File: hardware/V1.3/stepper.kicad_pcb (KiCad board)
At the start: 4 copper layers, 40 x 40 mm, 119 parts, among them J101 USB-MINI-B-SMD, J102 DRILL, J103 DRILL, J104 DRILL, J105 DRILL, J401 STACK-UP-HIGH, J402 STACK-DOWN, J403 STACK-UP-HIGH, J404 STACK-DOWN, P201 black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

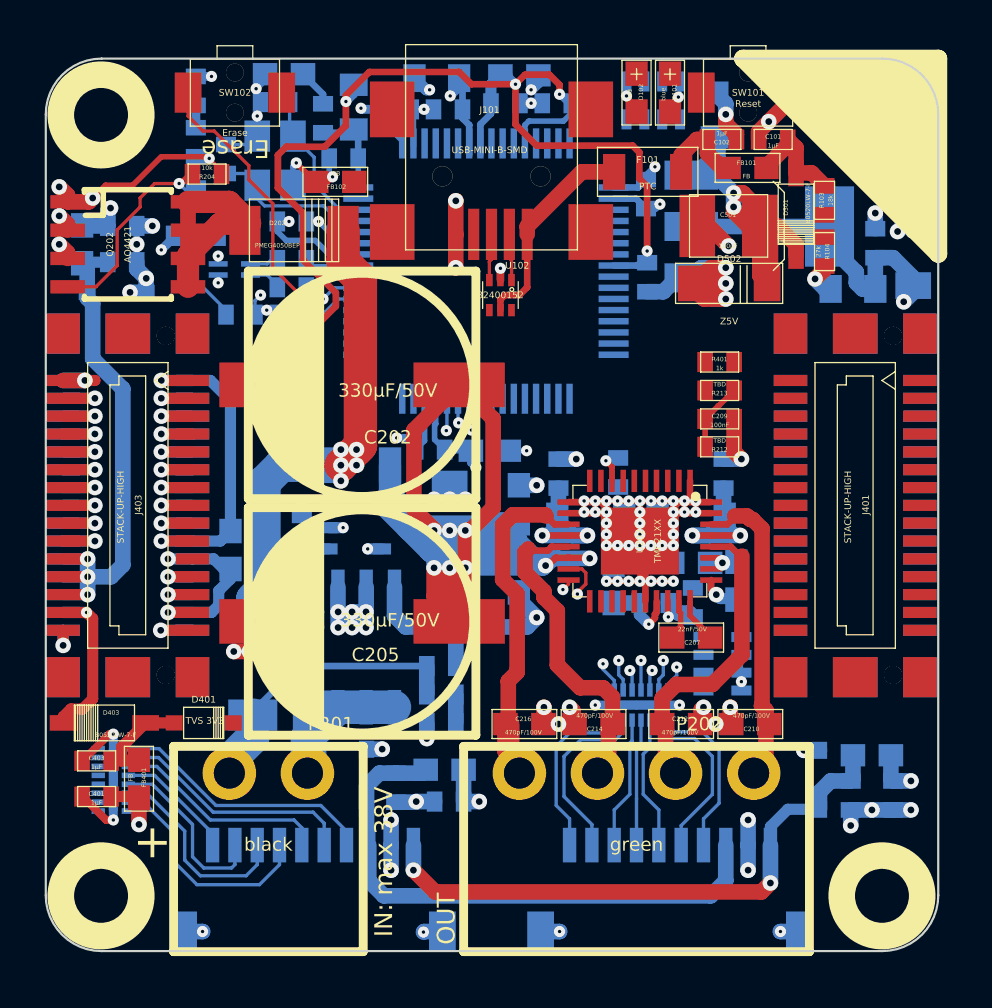
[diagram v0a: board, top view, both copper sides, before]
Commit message: fully routed, fine tuning missing
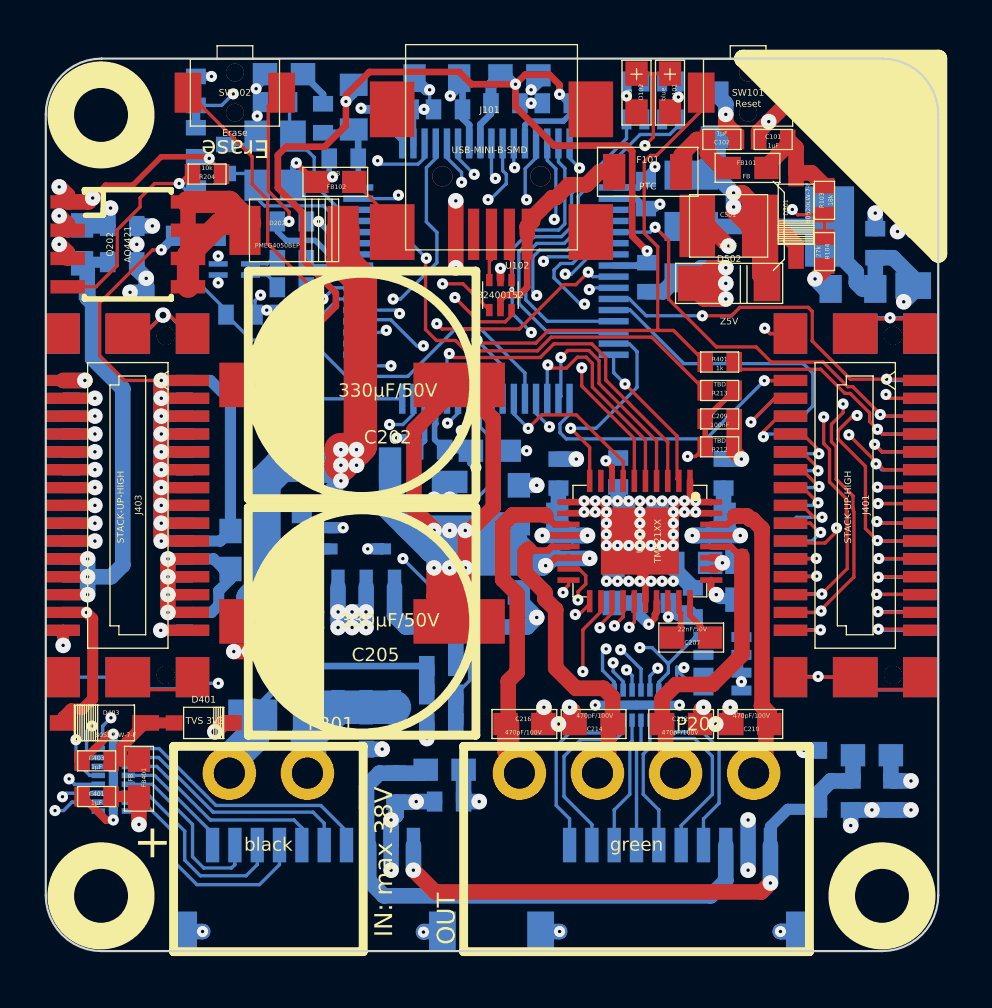
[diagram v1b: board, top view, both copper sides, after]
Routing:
- net GND: track 189.6 -> 402.5 mm, vias 57 -> 63
- net 3V3: track 44.6 -> 192.9 mm, vias 12 -> 14
- net BRICKLET-I2C-SCL: track 1.19 -> 54.6 mm, vias 1 -> 3
- net BRICKLET-I2C-SDA: track 2.35 -> 53.6 mm, vias 2 -> 3
- net BRICKLET-IO0_0/AD0: track 0.00 -> 45.8 mm, vias 0 -> 2
- net BRICKLET-IO1_0/AD1: track 1.33 -> 45.4 mm, vias 1 -> 2
- net BRICKLET-IO0_1: track 0.00 -> 42.0 mm, vias 0 -> 2
- net STACK-INT: track 0.00 -> 40.3 mm, vias 0 -> 3
- net BRICKLET-IO0_3: track 0.00 -> 39.4 mm, vias 0 -> 3
- net STACK-PGND: track 178.0 -> 217.1 mm, vias 78 -> 77
- net STACK-SER-RXD: track 0.00 -> 35.5 mm, vias 0 -> 3
- net STACK-SER-TXD: track 0.00 -> 35.2 mm, vias 0 -> 3
- net BRICKLET-IO1_1: track 0.92 -> 36.0 mm, vias 1 -> 2
- net BRICKLET-IO1_3: track 1.38 -> 33.8 mm, vias 1 -> 2
- net PWR-ENABLE: track 0.00 -> 31.4 mm, vias 0 -> 2
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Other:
- net class Default: trace_width 0.14986 -> 0.148
- rule trace_min: 0.14986 -> 0.148

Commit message: fully routed, logos etc. placed, finished
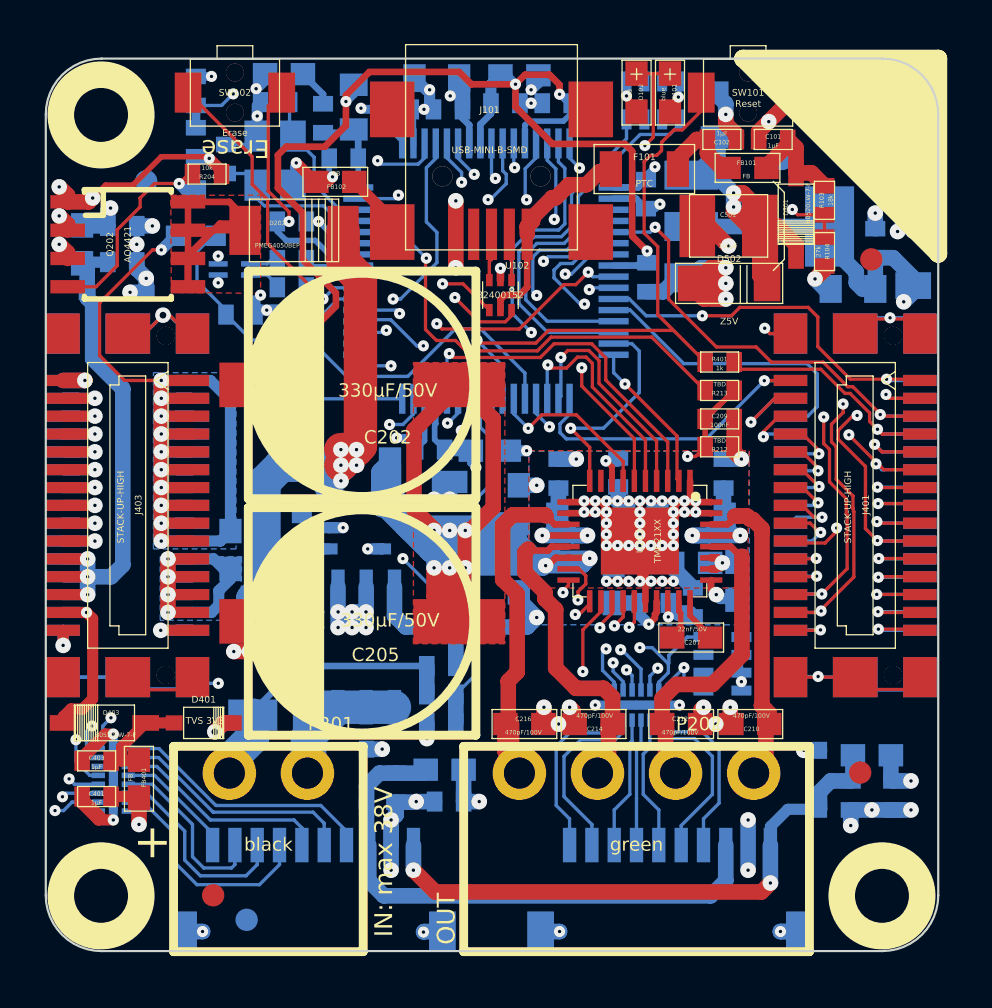
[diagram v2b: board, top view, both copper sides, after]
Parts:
- added Fiducial_Mark: VAL**, kicad-libraries:Fiducial_Mark, F.Cu at (163.7, 81.8)
- added Fiducial_Mark: VAL**, kicad-libraries:Fiducial_Mark, B.Cu at (135.7, 111.4)
- added Fiducial_Mark: VAL**, kicad-libraries:Fiducial_Mark, B.Cu at (131.2, 78.3)
- added Fiducial_Mark: VAL**, kicad-libraries:Fiducial_Mark, B.Cu at (159.7, 77.3)
- added Fiducial_Mark: VAL**, kicad-libraries:Fiducial_Mark, F.Cu at (163.2, 104.8)
- added Fiducial_Mark: VAL**, kicad-libraries:Fiducial_Mark, F.Cu at (134.2, 110.3)
- added G***: LOGO, kicad-libraries:Logo_31x31m, B.Cu at (157.5, 85.2)
- added VAL: WEEE_7mm_back, kicad-libraries:WEEE_7mm_back, B.Cu at (136.3, 88.3)
- added VAL: CE_5mm, kicad-libraries:CE_5mm, B.Cu at (148.4, 101.1)
- moved F101 0.20 mm to (153.6, 77.7)
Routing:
- net GND: track 402.5 -> 435.4 mm
- net VEE: track 73.7 -> 77.8 mm
- net Net-(D202-Pad2): track 28.2 -> 30.2 mm
- net 3V3: track 192.9 -> 192.0 mm
- net BRICKLET-IO1_0/AD1: track 45.4 -> 46.0 mm
- net BRICKLET-I2C-SDA: track 53.6 -> 54.2 mm
- net Net-(L101-Pad3): track 14.6 -> 15.1 mm
- net STACK-RESET: track 26.3 -> 26.8 mm
- added copper zone on VCC, net 3V3
- added copper zone on B.Cu, net GND
- added copper zone on GND, net GND
- added copper zone on F.Cu, net Net-(D202-Pad1)
- added copper zone on B.Cu, net STACK-PGND
- added copper zone on F.Cu, net STACK-PGND
- added copper zone on GND, net STACK-PGND
- added copper zone on VCC, net STACK-PVCC
- added copper zone on F.Cu, net VEE
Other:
- board text added: "tinkerforge.com"
- board text removed: "Reset"

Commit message: ordered version
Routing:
- net M2: track 14.5 -> 15.5 mm
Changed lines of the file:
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@@
     (thickness 1.6002)
     (drawings 64)
-    (tracks 2583)
+    (tracks 2589)
     (zones 0)
     (modules 128)
@@
     (1 GND signal hide)
     (2 VCC signal hide)
-    (31 Rückseite signal hide)
+    (31 Rückseite signal)
     (32 B.Adhes user)
     (33 F.Adhes user)
@@
   )
   (setup
-    (last_trace_width 0.1524)
+    (last_trace_width 0.25)
     (user_trace_width 0.1524)
     (user_trace_width 0.25)
@@
     (pad_to_mask_clearance 0)
     (aux_axis_origin 126.72568 112.776)
-    (visible_elements FFFF5FBF)
+    (visible_elements FFFF9FBF)
     (pcbplotparams
-      (layerselection 0x00030_80000001)
+      (layerselection 0x010f0_80000007)
       (usegerberextensions true)
       (excludeedgelayer true)
       (linewidth 0.150000)
-      (plotframeref true)
+      (plotframeref false)
       (viasonmask false)
       (mode 1)
@@
       (drillshape 0)
       (scaleselection 1)
-      (outputdirectory prod/))
+      (outputdirectory /tmp/stepper/))
   )
   (net 0 "")
@@
   (segment (start 139.15 74.8) (end 139.15 74.3749) (width 0.2998) (layer Rückseite) (net 123))
   (segment (start 139.05 74.6499) (end 139.2 74.8) (width 0.2998) (layer Rückseite) (net 123))
+  (segment (start 157.15 93.6507) (end 157.5257 93.275) (width 0.35) (layer Vorderseite) (net 124))
+  (segment (start 157.6 93.275) (end 157.8 93.275) (width 0.701) (layer Vorderseite) (net 124))
+  (segment (start 157.5257 93.275) (end 157.6 93.275) (width 0.35) (layer Vorderseite) (net 124))
   (segment (start 159.1501 102.6) (end 159.1501 102.1251) (width 0.70104) (layer Vorderseite) (net 124))
   (segment (start 159.1501 102.1251) (end 158.8 101.775) (width 0.70104) (layer Vorderseite) (net 124))
@@
   (segment (start 158.3 93.425) (end 158.3 93.5) (width 0.1524) (layer Vorderseite) (net 124))
   (segment (start 158.3 93.5) (end 158.825 94.025) (width 0.1524) (layer Vorderseite) (net 124))
-  (segment (start 156.54786 93.6507) (end 157.4243 93.6507) (width 0.1524) (layer Vorderseite) (net 124))
-  (segment (start 157.4243 93.6507) (end 157.8 93.275) (width 0.1524) (layer Vorderseite) (net 124))
+  (segment (start 156.54786 93.6507) (end 157.15 93.6507) (width 0.1524) (layer Vorderseite) (net 124))
   (segment (start 158.4 93.425) (end 158.3 93.425) (width 0.701) (layer Vorderseite) (net 124))
   (segment (start 158.15 93.275) (end 157.8 93.275) (width 0.701) (layer Vorderseite) (net 124))
-  (segment (start 157.8 93.275) (end 157.6 93.275) (width 0.701) (layer Vorderseite) (net 124))
   (segment (start 158.3 93.425) (end 158.15 93.275) (width 0.701) (layer Vorderseite) (net 124))
   (segment (start 159 104.25) (end 158.45 104.8) (width 0.701) (layer Vorderseite) (net 124))
@@
   (segment (start 158.4 93.425) (end 158.3 93.425) (width 0.2998) (layer Vorderseite) (net 124))
   (segment (start 158.3 93.425) (end 158.05 93.425) (width 0.2998) (layer Vorderseite) (net 124))
+  (segment (start 157.925 95.25) (end 157.325 94.65) (width 0.35) (layer Vorderseite) (net 125))
+  (segment (start 157.175 94.65) (end 157.175 94.6489) (width 0.35) (layer Vorderseite) (net 125))
+  (segment (start 157.325 94.65) (end 157.175 94.65) (width 0.35) (layer Vorderseite) (net 125))
   (segment (start 154.5 104.35) (end 154.95 104.8) (width 0.701) (layer Vorderseite) (net 125))
   (segment (start 154.5 102.6) (end 154.5 104.35) (width 0.701) (layer Vorderseite) (net 125))
-  (segment (start 157.85 95.075) (end 157.925 95.075) (width 0.2998) (layer Vorderseite) (net 125))
-  (segment (start 157.424 94.6489) (end 157.85 95.075) (width 0.2998) (layer Vorderseite) (net 125))
-  (segment (start 156.548 94.6489) (end 157.424 94.6489) (width 0.2998) (layer Vorderseite) (net 125))
+  (segment (start 156.548 94.6489) (end 157.175 94.6489) (width 0.2998) (layer Vorderseite) (net 125))
   (segment (start 154.35 101.45) (end 154.35 102.425) (width 0.701) (layer Vorderseite) (net 125))
   (segment (start 154.975 100.825) (end 154.35 101.45) (width 0.701) (layer Vorderseite) (net 125))
   (segment (start 156.6 100.825) (end 154.975 100.825) (width 0.701) (layer Vorderseite) (net 125))
   (segment (start 157.925 99.5) (end 156.6 100.825) (width 0.701) (layer Vorderseite) (net 125))
-  (segment (start 157.925 95.075) (end 157.925 99.5) (width 0.701) (layer Vorderseite) (net 125))
+  (segment (start 157.925 95.25) (end 157.925 99.5) (width 0.701) (layer Vorderseite) (net 125))
+  (segment (start 148.2 95.8) (end 148.425 95.575) (width 0.25) (layer Vorderseite) (net 126))
+  (segment (start 148.425 95.225) (end 148.675 94.975) (width 0.25) (layer Vorderseite) (net 126))
+  (segment (start 148.425 95.575) (end 148.425 95.225) (width 0.25) (layer Vorderseite) (net 126))
   (segment (start 149.401 94.6489) (end 150.152 94.6489) (width 0.2998) (layer Vorderseite) (net 126))
   (segment (start 149.225 94.825) (end 149.401 94.6489) (width 0.2998) (layer Vorderseite) (net 126))
@@
   (segment (start 149.0916 96.9881) (end 149.5764 97.4729) (width 0.701) (layer Vorderseite) (net 126))
   (segment (start 149.0916 96.6916) (end 149.0916 96.9881) (width 0.701) (layer Vorderseite) (net 126))
+  (segment (start 148.2 95.8) (end 148.2 95.8) (width 0.701) (layer Vorderseite) (net 126))
   (segment (start 148.2 95.8) (end 149.0916 96.6916) (width 0.701) (layer Vorderseite) (net 126))
   (segment (start 148.2 94.9) (end 148.2 95.8) (width 0.701) (layer Vorderseite) (net 126))
